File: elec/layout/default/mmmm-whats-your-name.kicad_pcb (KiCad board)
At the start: 2 copper layers, 40 x 40 mm, 142 parts

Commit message: Placement done!
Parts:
- added C25: Multilayer Ceramic Capacitors MLCC - SMD/SMT 2.2uF 10V 0603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, lib:C0603, F.Cu at (85.0, 42.8)
- added C26: Multilayer Ceramic Capacitors MLCC - SMD/SMT 2.2uF 10V 0603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, lib:C0603, F.Cu at (116.0, 42.8)
- added C27: Multilayer Ceramic Capacitors MLCC - SMD/SMT 2.2uF 10V 0603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, lib:C0603, F.Cu at (85.0, 45.8)
- added C28: Multilayer Ceramic Capacitors MLCC - SMD/SMT 2.2uF 10V 0603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, lib:C0603, F.Cu at (116.0, 45.9)
- added C29: Multilayer Ceramic Capacitors MLCC - SMD/SMT 2.2uF 10V 0603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, lib:C0603, F.Cu at (85.0, 48.9)
- added C30: Multilayer Ceramic Capacitors MLCC - SMD/SMT 2.2uF 10V 0603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, lib:C0603, F.Cu at (116.0, 48.9)
- added C31: Multilayer Ceramic Capacitors MLCC - SMD/SMT 2.2uF 10V 0603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, lib:C0603, F.Cu at (85.0, 52.0)
- added C32: Multilayer Ceramic Capacitors MLCC - SMD/SMT 2.2uF 10V 0603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, lib:C0603, F.Cu at (116.0, 52.0)
- added C33: Multilayer Ceramic Capacitors MLCC - SMD/SMT 2.2uF 10V 0603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, lib:C0603, F.Cu at (85.0, 55.0)
- added C34: Multilayer Ceramic Capacitors MLCC - SMD/SMT 2.2uF 10V 0603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, lib:C0603, F.Cu at (116.0, 55.0)
- added C35: Multilayer Ceramic Capacitors MLCC - SMD/SMT 2.2uF 10V 0603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, lib:C0603, F.Cu at (85.0, 58.1)
- added C36: Multilayer Ceramic Capacitors MLCC - SMD/SMT 2.2uF 10V 0603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, lib:C0603, F.Cu at (116.0, 58.1)
- added C37: Multilayer Ceramic Capacitors MLCC - SMD/SMT 2.2uF 10V 0603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, lib:C0603, F.Cu at (85.0, 61.1)
- added C38: Multilayer Ceramic Capacitors MLCC - SMD/SMT 2.2uF 10V 0603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, lib:C0603, F.Cu at (116.0, 61.1)
- added C39: Multilayer Ceramic Capacitors MLCC - SMD/SMT 2.2uF 10V 0603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, lib:C0603, F.Cu at (85.0, 64.1)
- added C40: Multilayer Ceramic Capacitors MLCC - SMD/SMT 2.2uF 10V 0603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, lib:C0603, F.Cu at (116.0, 64.1)
- added C41: Multilayer Ceramic Capacitors MLCC - SMD/SMT 2.2uF 10V 0603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, lib:C0603, F.Cu at (85.0, 67.2)
- added C42: Multilayer Ceramic Capacitors MLCC - SMD/SMT 2.2uF 10V 0603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, lib:C0603, F.Cu at (116.0, 67.2)
- added C43: Multilayer Ceramic Capacitors MLCC - SMD/SMT 2.2uF 10V 0603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, lib:C0603, F.Cu at (98.2, 73.4)
- added C44: Multilayer Ceramic Capacitors MLCC - SMD/SMT 2.2uF 10V 0603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, lib:C0603, F.Cu at (126.5, 73.8)
- moved U33 359.2 mm to (105.8, 48.9)
- moved U59 352.6 mm to (102.7, 57.8)
- moved U26 347.3 mm to (111.9, 45.8)
- moved U55 337.8 mm to (90.5, 57.8)
- moved U78 336.7 mm to (105.8, 63.6)
- moved U35 326.9 mm to (111.9, 48.9)
- moved U24 323.9 mm to (105.8, 45.8)
- moved U93 318.0 mm to (109.3, 76.1)
- moved U91 317.3 mm to (95.2, 76.1)
- moved U45 311.9 mm to (87.5, 54.9)
- moved U51 311.5 mm to (105.8, 54.9)
- moved U54 308.7 mm to (87.5, 57.8)
- moved U47 305.6 mm to (93.6, 54.9)
- moved U64 305.4 mm to (90.5, 60.7)
- moved U48 301.7 mm to (96.6, 54.9)
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
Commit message: Layout's done!
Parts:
- moved U5 29.6 mm to (136.7, 69.1)
- moved C11 29.6 mm to (137.4, 70.8)
- moved C12 29.6 mm to (137.4, 67.4)
- moved LED2 29.6 mm to (138.0, 66.0)
- moved R10 29.6 mm to (134.0, 67.8)
- moved LED1 29.6 mm to (135.1, 66.0)
- moved R11 29.6 mm to (138.8, 67.9)
- moved R9 29.6 mm to (135.5, 67.3)
- moved C41 24.7 mm to (83.4, 42.6), turned to -90 degrees
- moved C25 24.2 mm to (83.4, 67.0), turned to -90 degrees
- moved C39 18.6 mm to (83.4, 45.6), turned to -90 degrees
- moved C9 18.6 mm to (118.4, 66.7), turned to 90 degrees
- moved C27 18.2 mm to (83.4, 63.9), turned to -90 degrees
- moved C8 14.7 mm to (120.4, 66.7), turned to 90 degrees
- moved C37 12.5 mm to (83.4, 48.7), turned to -90 degrees
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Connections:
- U1 pad 1: vcc -> gnd
- U1 pad 2: gnd -> vcc
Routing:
- net vcc-2: track 6.20 -> 169.1 mm, vias 0 -> 129
- net gpio17: track 0.00 -> 67.6 mm, vias 0 -> 2
- net gpio16: track 0.00 -> 63.0 mm, vias 0 -> 2
- net vcc-3: track 6.03 -> 40.2 mm
- net vcc-8: track 0.00 -> 32.7 mm, vias 0 -> 2
- net vcc-62: track 0.00 -> 32.5 mm, vias 0 -> 2
- net vcc-26: track 0.00 -> 32.5 mm, vias 0 -> 2
- net vcc-35: track 0.00 -> 32.4 mm, vias 0 -> 2
- net vcc-17: track 0.00 -> 32.4 mm, vias 0 -> 2
- net vcc-53: track 0.00 -> 32.1 mm, vias 0 -> 2
- net vcc-44: track 0.00 -> 32.1 mm, vias 0 -> 2
- net vcc-71: track 0.00 -> 31.8 mm, vias 0 -> 2
- net vcc: track 15.4 -> 38.8 mm, vias 0 -> 2
- net run: track 0.00 -> 13.0 mm, vias 0 -> 2
- net vcc-1: track 48.7 -> 60.2 mm
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- added copper zone on F.Cu, net gnd
- added copper zone on In1.Cu, net gnd
- added copper zone on B.Cu, net vcc-2
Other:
- board size 40 x 40 mm -> 61.1 x 48.9 mm
- copper layers 2 -> 4
- board text added: "+"
- board text added: "-"

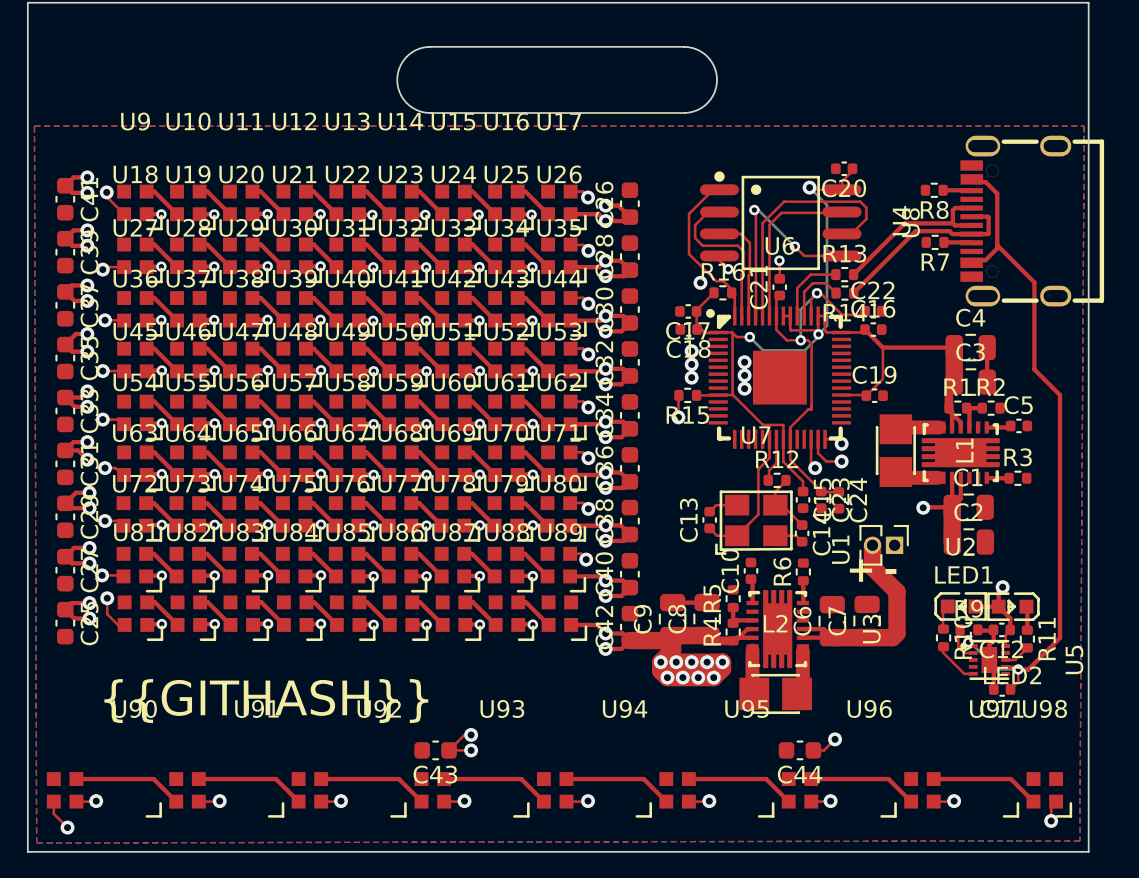
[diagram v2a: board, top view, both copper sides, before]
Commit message: Add reset/boot buttons
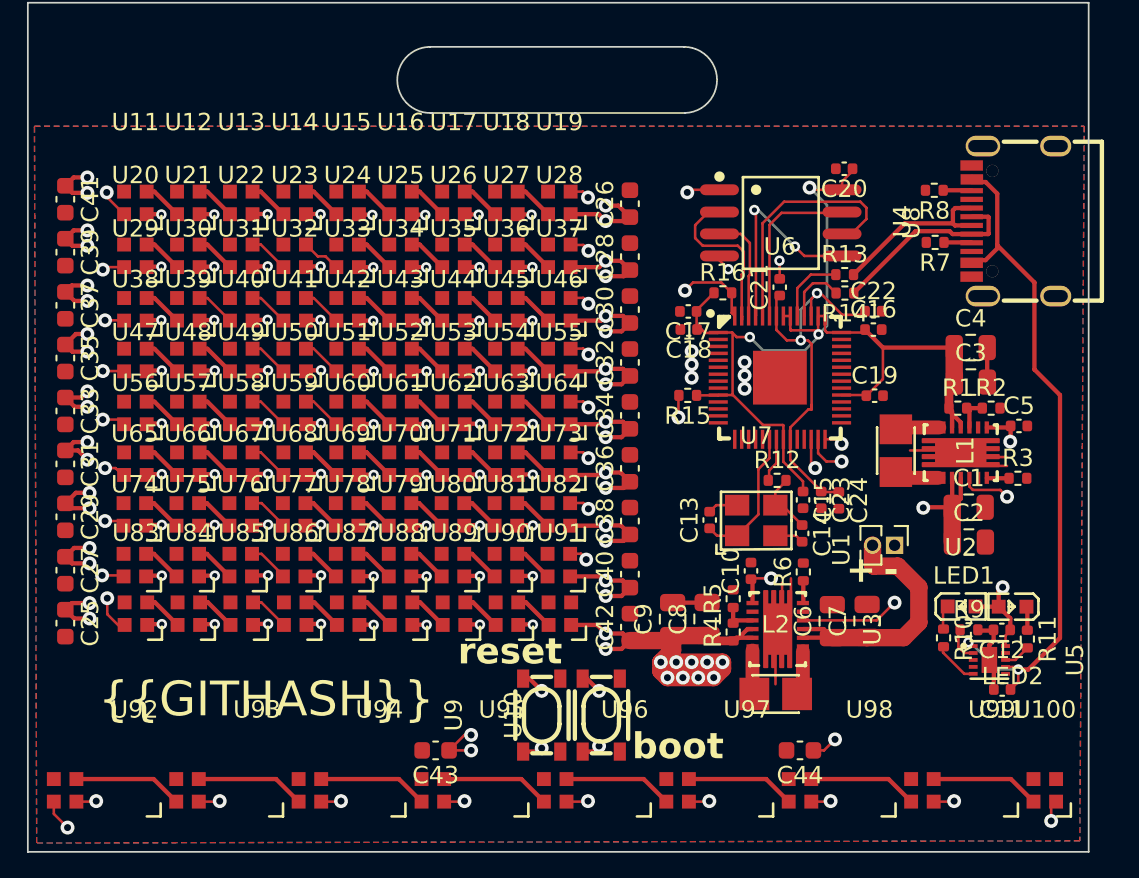
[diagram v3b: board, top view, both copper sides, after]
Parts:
- added U10: , lib:KEY-SMD_4P-L4.2-W3.2-P2.20-LS4.6, F.Cu at (114.3, 72.3)
- added U9: , lib:KEY-SMD_4P-L4.2-W3.2-P2.20-LS4.6, F.Cu at (110.9, 72.3)
- renumbered U98 to U100, U9 to U11, U10 to U12, U11 to U13, U12 to U14, U13 to U15, U14 to U16, U15 to U17, U16 to U18, U17 to U19, U18 to U20, U19 to U21, U20 to U22, U21 to U23, U22 to U24, U23 to U25, U24 to U26, U25 to U27, U26 to U28, U27 to U29, U28 to U30, U29 to U31, U30 to U32, U31 to U33, U32 to U34, U33 to U35, U34 to U36, U35 to U37, U36 to U38, U37 to U39, U38 to U40, U39 to U41, U40 to U42, U41 to U43, U42 to U44, U43 to U45, U44 to U46, U45 to U47, U46 to U48, U47 to U49, U48 to U50, U49 to U51, U50 to U52, U51 to U53, U52 to U54, U53 to U55, U54 to U56, U55 to U57, U56 to U58, U57 to U59, U58 to U60, U59 to U61, U60 to U62, U61 to U63, U62 to U64, U63 to U65, U64 to U66, U65 to U67, U66 to U68, U67 to U69, U68 to U70, U69 to U71, U70 to U72, U71 to U73, U72 to U74, U73 to U75, U74 to U76, U75 to U77, U76 to U78, U77 to U79, U78 to U80, U79 to U81, U80 to U82, U81 to U83, U82 to U84, U83 to U85, U84 to U86, U85 to U87, U86 to U88, U87 to U89, U88 to U90, U89 to U91, U90 to U92, U91 to U93, U92 to U94, U93 to U95, U94 to U96, U95 to U97, U96 to U98, U97 to U99
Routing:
- net cs: track 9.55 -> 44.4 mm, vias 0 -> 4
- net run: track 13.0 -> 39.2 mm, vias 2 -> 4
- net gnd: track 15.9 -> 31.7 mm, vias 9 -> 8
- net vina-1: track 1.41 -> 16.0 mm, vias 0 -> 2
- net vina: track 1.41 -> 8.48 mm, vias 0 -> 2
- net vcc-28: track 0.00 -> 2.29 mm
- net vcc: track 38.8 -> 41.0 mm
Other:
- board text added: "boot"
- board text added: "reset"

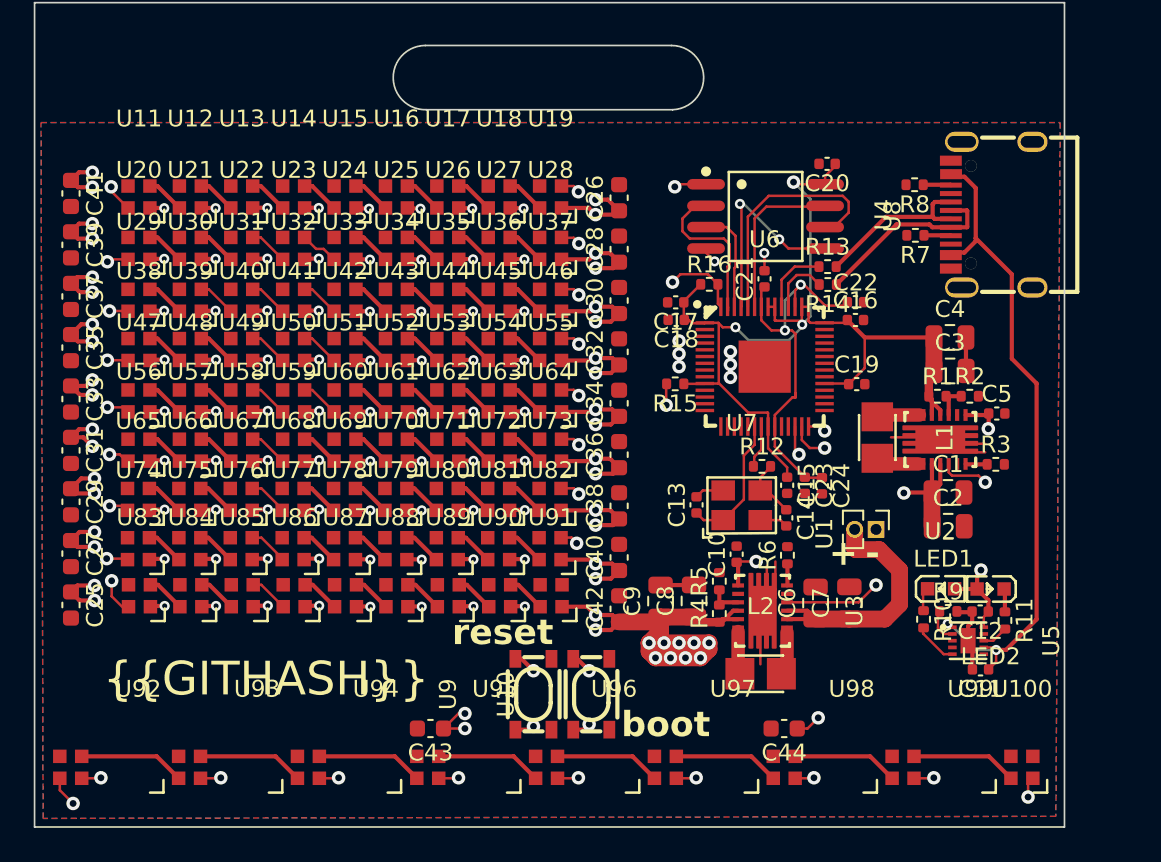
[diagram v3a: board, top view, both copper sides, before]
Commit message: This commit does a couple of semi-questionable things: 1. I add two footprints/modules directly to the repo I don't think I need 2. I ungrouped everything (which screws up the sync to the other layouts) to remove the text from things
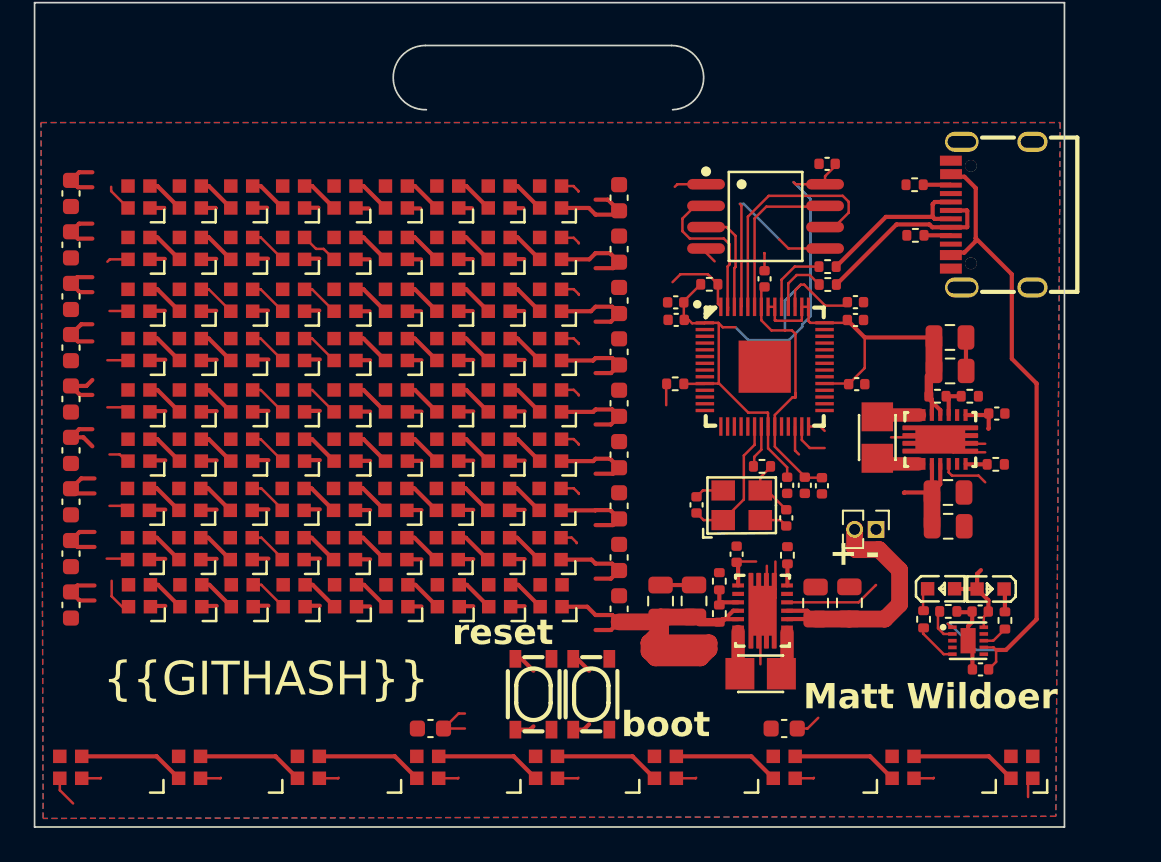
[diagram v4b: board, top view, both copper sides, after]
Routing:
- net vina-1: vias 2 -> 0
- net vina: vias 2 -> 0
- net vcc-8: vias 2 -> 0
- net vcc-71: vias 2 -> 0
- net vcc-62: vias 2 -> 0
- net vcc-6: vias 2 -> 0
- net vcc-53: vias 2 -> 0
- net vcc-44: vias 2 -> 0
- net vcc-35: vias 2 -> 0
- net vcc-3: vias 2 -> 0
- net vcc-26: vias 2 -> 0
- net vcc-2: vias 129 -> 0
- net vcc-17: vias 2 -> 0
- net vcc-1: vias 3 -> 0
- net vcc: vias 2 -> 0
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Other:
- board text added: "Matt Wildoer"

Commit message: Nice edges
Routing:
- net vina-1: vias 0 -> 2
- net vina: vias 0 -> 2
- net vcc-8: vias 0 -> 2
- net vcc-71: vias 0 -> 2
- net vcc-62: vias 0 -> 2
- net vcc-6: vias 0 -> 2
- net vcc-53: vias 0 -> 2
- net vcc-44: vias 0 -> 2
- net vcc-35: vias 0 -> 2
- net vcc-3: vias 0 -> 2
- net vcc-26: vias 0 -> 2
- net vcc-2: vias 0 -> 129
- net vcc-17: vias 0 -> 2
- net vcc-1: vias 0 -> 3
- net vcc: vias 0 -> 2
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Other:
- outline, holes or cut-outs redrawn
